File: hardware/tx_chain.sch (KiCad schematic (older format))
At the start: 34 parts

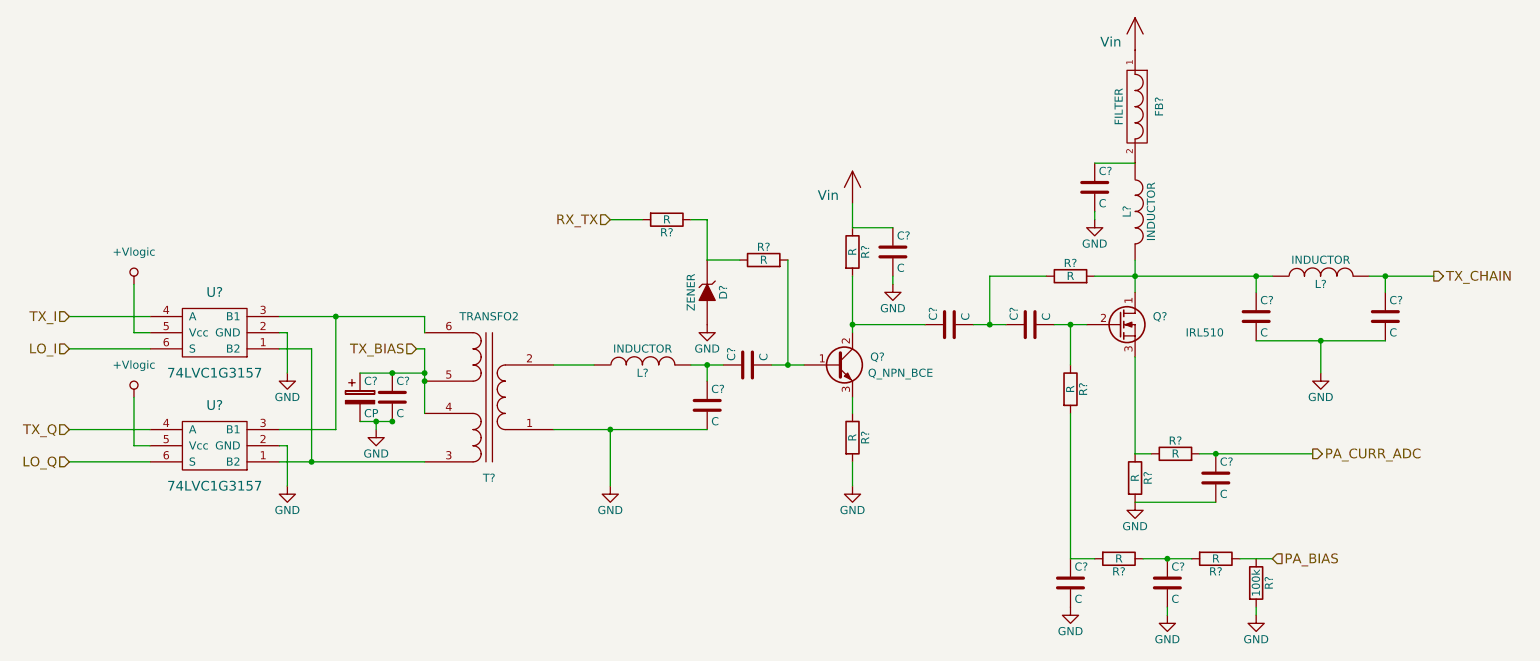
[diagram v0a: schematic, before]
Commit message: Added annotation so willing prove readers can reference components more easily
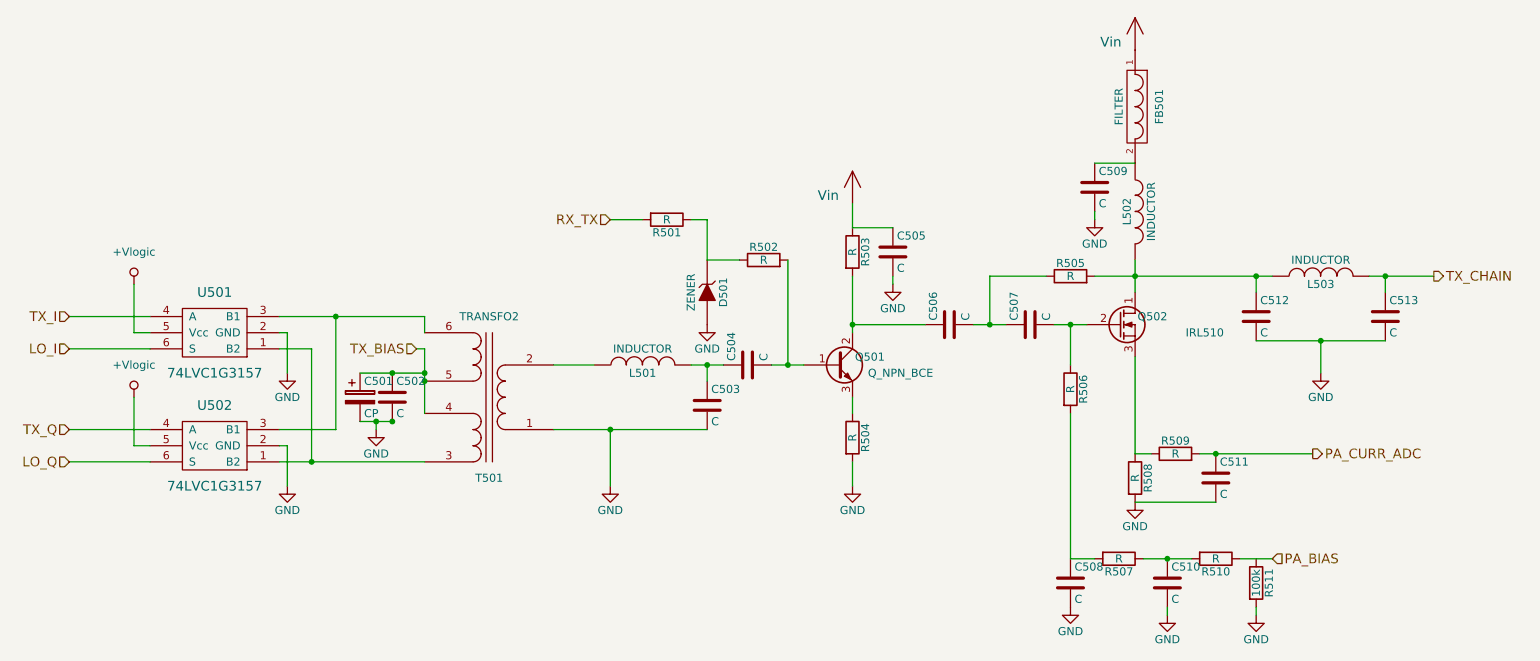
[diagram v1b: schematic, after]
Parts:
- gave numbers to parts that had none: 34

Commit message: fixed some more ERC errors
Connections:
- net PA_BIAS: now also R511.1
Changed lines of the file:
@@
 $EndComp
 $Comp
-L GND #PWR018
+L GND #PWR021
 U 1 1 57E4343C
 P 3100 4100
-F 0 "#PWR018" H 3100 3850 50  0001 C CNN
+F 0 "#PWR021" H 3100 3850 50  0001 C CNN
 F 1 "GND" H 3100 3950 50  0000 C CNN
 F 2 "" H 3100 4100 50  0000 C CNN
@@
 $EndComp
 $Comp
-L GND #PWR019
+L GND #PWR022
 U 1 1 57E4345E
 P 3100 4800
-F 0 "#PWR019" H 3100 4550 50  0001 C CNN
+F 0 "#PWR022" H 3100 4550 50  0001 C CNN
 F 1 "GND" H 3100 4650 50  0000 C CNN
 F 2 "" H 3100 4800 50  0000 C CNN
@@
 $EndComp
 $Comp
-L +Vlogic #PWR020
+L +Vlogic #PWR023
 U 1 1 57E434AC
 P 2150 3550
-F 0 "#PWR020" H 2150 3350 50  0001 C CNN
+F 0 "#PWR023" H 2150 3350 50  0001 C CNN
 F 1 "+Vlogic" H 2150 3750 50  0000 C CNN
 F 2 "" H 2150 3550 50  0000 C CNN
@@
 $EndComp
 $Comp
-L +Vlogic #PWR021
+L +Vlogic #PWR024
 U 1 1 57E434C4
 P 2150 4250
-F 0 "#PWR021" H 2150 4050 50  0001 C CNN
+F 0 "#PWR024" H 2150 4050 50  0001 C CNN
 F 1 "+Vlogic" H 2150 4450 50  0000 C CNN
 F 2 "" H 2150 4250 50  0000 C CNN
@@
 $EndComp
 $Comp
-L GND #PWR022
+L GND #PWR025
 U 1 1 57E43B57
 P 3650 4450
-F 0 "#PWR022" H 3650 4200 50  0001 C CNN
+F 0 "#PWR025" H 3650 4200 50  0001 C CNN
 F 1 "GND" H 3650 4300 50  0000 C CNN
 F 2 "" H 3650 4450 50  0000 C CNN
@@
 $EndComp
 $Comp
-L GND #PWR023
+L GND #PWR026
 U 1 1 57E43B98
 P 5100 4800
-F 0 "#PWR023" H 5100 4550 50  0001 C CNN
+F 0 "#PWR026" H 5100 4550 50  0001 C CNN
 F 1 "GND" H 5100 4650 50  0000 C CNN
 F 2 "" H 5100 4800 50  0000 C CNN
@@
 $EndComp
 $Comp
-L GND #PWR024
+L GND #PWR027
 U 1 1 57E44284
 P 6600 4800
-F 0 "#PWR024" H 6600 4550 50  0001 C CNN
+F 0 "#PWR027" H 6600 4550 50  0001 C CNN
 F 1 "GND" H 6600 4650 50  0000 C CNN
 F 2 "" H 6600 4800 50  0000 C CNN
@@
 $EndComp
 $Comp
-L Vin #Vin025
+L Vin #Vin028
 U 1 1 57E4514D
 P 6600 3050
-F 0 "#Vin025" H 6750 3100 60  0001 C CNN
+F 0 "#Vin028" H 6750 3100 60  0001 C CNN
 F 1 "Vin" H 6450 3100 60  0000 C CNN
 F 2 "" H 6600 3050 60  0001 C CNN
@@
 $EndComp
 $Comp
-L GND #PWR026
+L GND #PWR029
 U 1 1 57E451F7
 P 6850 3550
-F 0 "#PWR026" H 6850 3300 50  0001 C CNN
+F 0 "#PWR029" H 6850 3300 50  0001 C CNN
 F 1 "GND" H 6850 3400 50  0000 C CNN
 F 2 "" H 6850 3550 50  0000 C CNN
@@
 $EndComp
 $Comp
-L GND #PWR027
+L GND #PWR030
 U 1 1 57E458EE
 P 8100 3150
-F 0 "#PWR027" H 8100 2900 50  0001 C CNN
+F 0 "#PWR030" H 8100 2900 50  0001 C CNN
 F 1 "GND" H 8100 3000 50  0000 C CNN
 F 2 "" H 8100 3150 50  0000 C CNN
@@
 $EndComp
 $Comp
-L Vin #Vin028
+L Vin #Vin031
 U 1 1 57E45ADD
 P 8350 2100
-F 0 "#Vin028" H 8500 2150 60  0001 C CNN
+F 0 "#Vin031" H 8500 2150 60  0001 C CNN
 F 1 "Vin" H 8200 2150 60  0000 C CNN
 F 2 "" H 8350 2100 60  0001 C CNN
@@
 $EndComp
 $Comp
-L GND #PWR029
+L GND #PWR032
 U 1 1 57E45E2D
 P 8350 4900
-F 0 "#PWR029" H 8350 4650 50  0001 C CNN
+F 0 "#PWR032" H 8350 4650 50  0001 C CNN
 F 1 "GND" H 8350 4750 50  0000 C CNN
 F 2 "" H 8350 4900 50  0000 C CNN
@@
 $EndComp
 $Comp
-L GND #PWR030
+L GND #PWR033
 U 1 1 57E465CB
 P 9500 4100
-F 0 "#PWR030" H 9500 3850 50  0001 C CNN
+F 0 "#PWR033" H 9500 3850 50  0001 C CNN
 F 1 "GND" H 9500 3950 50  0000 C CNN
 F 2 "" H 9500 4100 50  0000 C CNN
@@
 $EndComp
 $Comp
-L GND #PWR031
+L GND #PWR034
 U 1 1 57E471D5
 P 5700 3800
-F 0 "#PWR031" H 5700 3550 50  0001 C CNN
+F 0 "#PWR034" H 5700 3550 50  0001 C CNN
 F 1 "GND" H 5700 3650 50  0000 C CNN
 F 2 "" H 5700 3800 50  0000 C CNN
@@
 $EndComp
 $Comp
-L GND #PWR032
+L GND #PWR035
 U 1 1 57EBA5D8
 P 7950 5550
-F 0 "#PWR032" H 7950 5300 50  0001 C CNN
+F 0 "#PWR035" H 7950 5300 50  0001 C CNN
 F 1 "GND" H 7950 5400 50  0000 C CNN
 F 2 "" H 7950 5550 50  0000 C CNN
@@
 $EndComp
 $Comp
-L GND #PWR033
+L GND #PWR036
 U 1 1 57EBA6B5
 P 8550 5600
-F 0 "#PWR033" H 8550 5350 50  0001 C CNN
+F 0 "#PWR036" H 8550 5350 50  0001 C CNN
 F 1 "GND" H 8550 5450 50  0000 C CNN
 F 2 "" H 8550 5600 50  0000 C CNN
@@
 $EndComp
 $Comp
-L GND #PWR034
+L GND #PWR037
 U 1 1 57EAC40D
 P 9100 5600
-F 0 "#PWR034" H 9100 5350 50  0001 C CNN
+F 0 "#PWR037" H 9100 5350 50  0001 C CNN
 F 1 "GND" H 9100 5450 50  0000 C CNN
 F 2 "" H 9100 5600 50  0000 C CNN
@@
 Wire Wire Line
 	9100 5600 9100 5550
+$Comp
+L PWR_FLAG #FLG038
+U 1 1 57EE98C9
+P 6900 3000
+F 0 "#FLG038" H 6900 3095 50  0001 C CNN
+F 1 "PWR_FLAG" H 6900 3180 50  0000 C CNN
+F 2 "" H 6900 3000 50  0000 C CNN
+F 3 "" H 6900 3000 50  0000 C CNN
+	1    6900 3000
+	1    0    0    -1
+$EndComp
+Wire Wire Line
+	6900 3000 6900 3100
+Wire Wire Line
+	6900 3100 6600 3100
+Connection ~ 6600 3100
+$Comp
+L PWR_FLAG #FLG039
+U 1 1 57EE999B
+P 8750 2100
+F 0 "#FLG039" H 8750 2195 50  0001 C CNN
+F 1 "PWR_FLAG" H 8750 2280 50  0000 C CNN
+F 2 "" H 8750 2100 50  0000 C CNN
+F 3 "" H 8750 2100 50  0000 C CNN
+	1    8750 2100
+	1    0    0    -1
+$EndComp
+Wire Wire Line
+	8750 2100 8350 2100
+Connection ~ 9100 5250
 $EndSCHEMATC

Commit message: Linked first components to footprints and updated schematic plot
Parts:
- C501, C502, C503, C504, C505, C506, C507, C508, C509, C510, C511, C512, C513: footprint (none) -> Capacitors_SMD:C_0805
- R501, R502, R503, R504, R505, R506, R507, R508, R509, R510, R511: footprint (none) -> Resistors_SMD:R_0805_HandSoldering

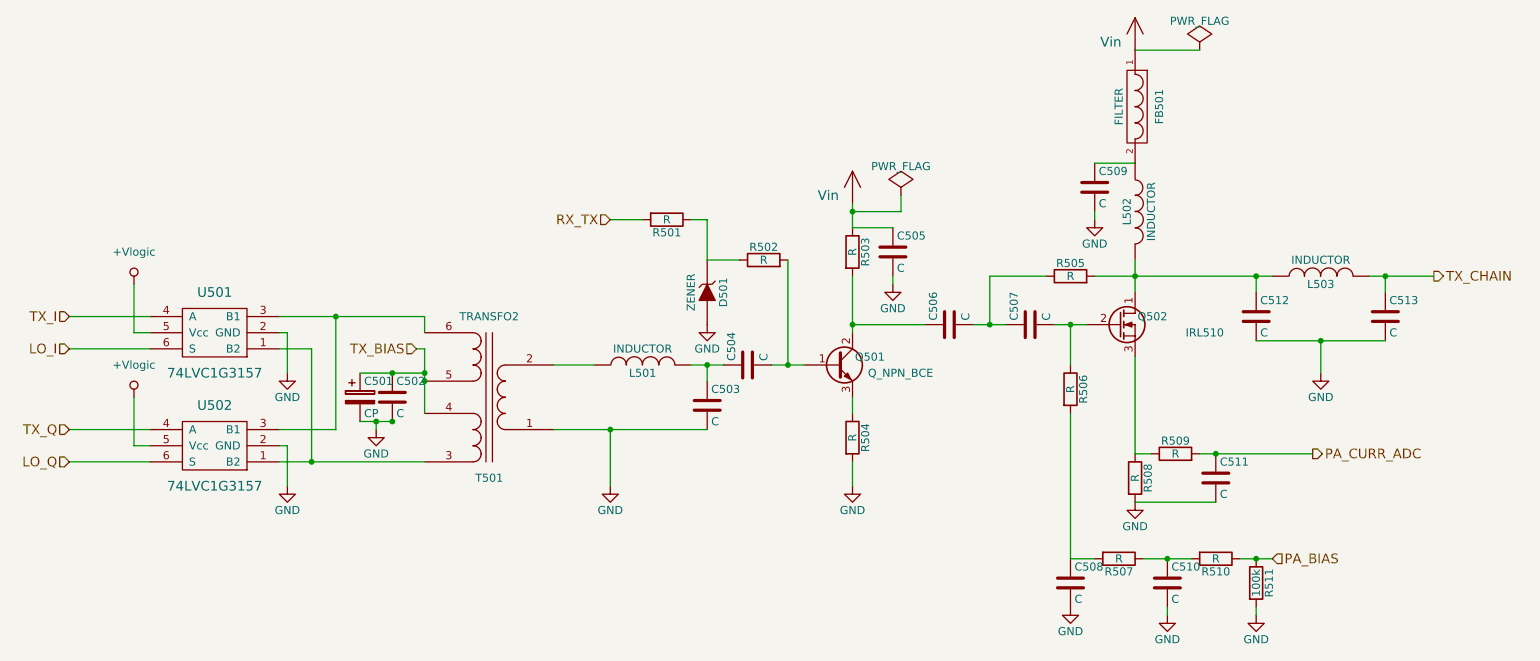
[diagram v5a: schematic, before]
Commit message: Changed SWR microstrip for two transformers and gave missing values for components
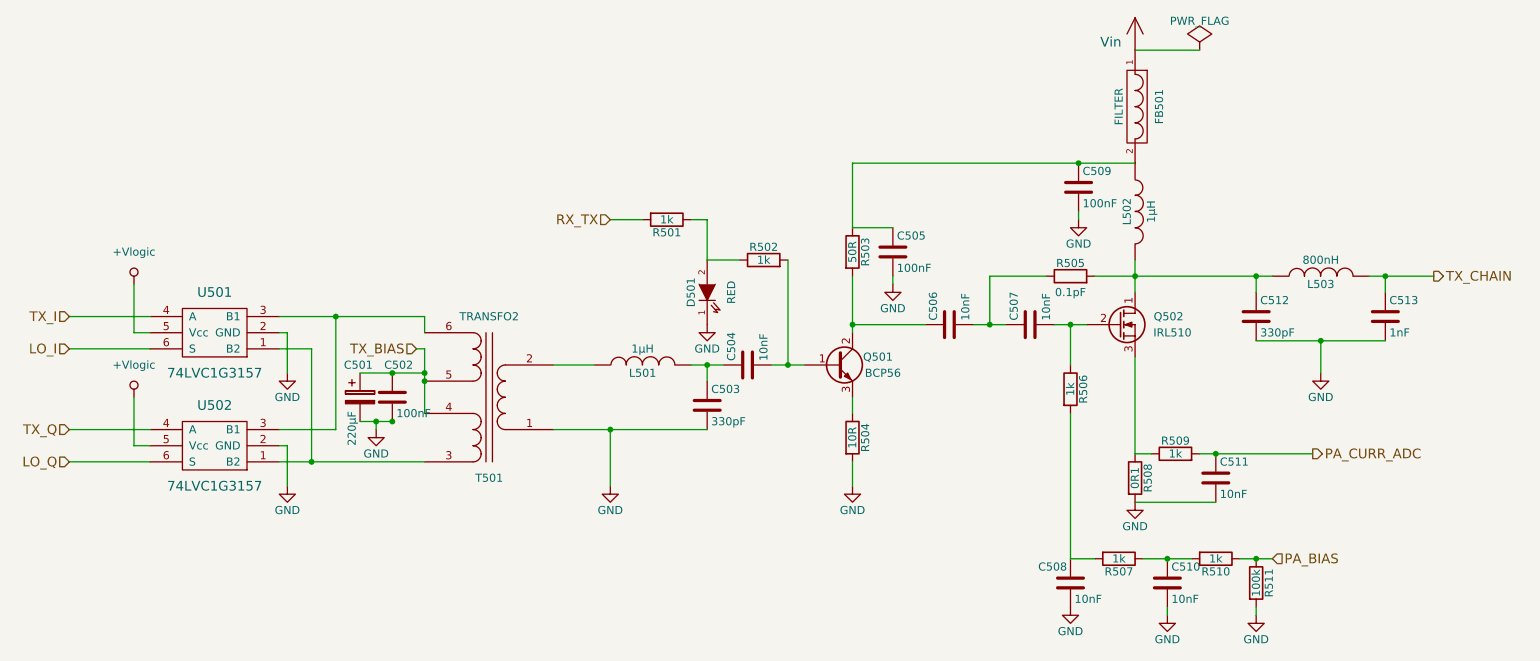
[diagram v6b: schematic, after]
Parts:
- removed D501: ZENER, symbol ZENER
- added D501: RED, symbol LED
- C501: value CP -> 220µF
- C502, C505, C509: value C -> 100nF
- C503, C512: value C -> 330pF
- C504, C506, C507, C508, C510, C511: value C -> 10nF
- C513: value C -> 1nF
- L501, L502: value INDUCTOR -> 1µH
- L503: value INDUCTOR -> 800nH
- Q501: value Q_NPN_BCE -> BCP56
- R501, R502, R506, R507, R509, R510: value R -> 1k
- R503: value R -> 50R
- R504: value R -> 10R
- R505: value R -> 0.1pF
- R508: value R -> 0R1
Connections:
- net GND: now also D501.1 (K)
- net at C505.1, R503.1: now also C509.1, FB501.2, L502.1
- net at R501.1, R502.1: now also D501.2 (A)
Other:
- moved on the sheet: C509
